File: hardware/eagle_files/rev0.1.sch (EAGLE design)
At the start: 30 parts, among them U1 AD8332ACPZ-R7, U2 AD8333ACPZ-REEL, U3 AD8021ARMZ, U4 AD8021ARMZ

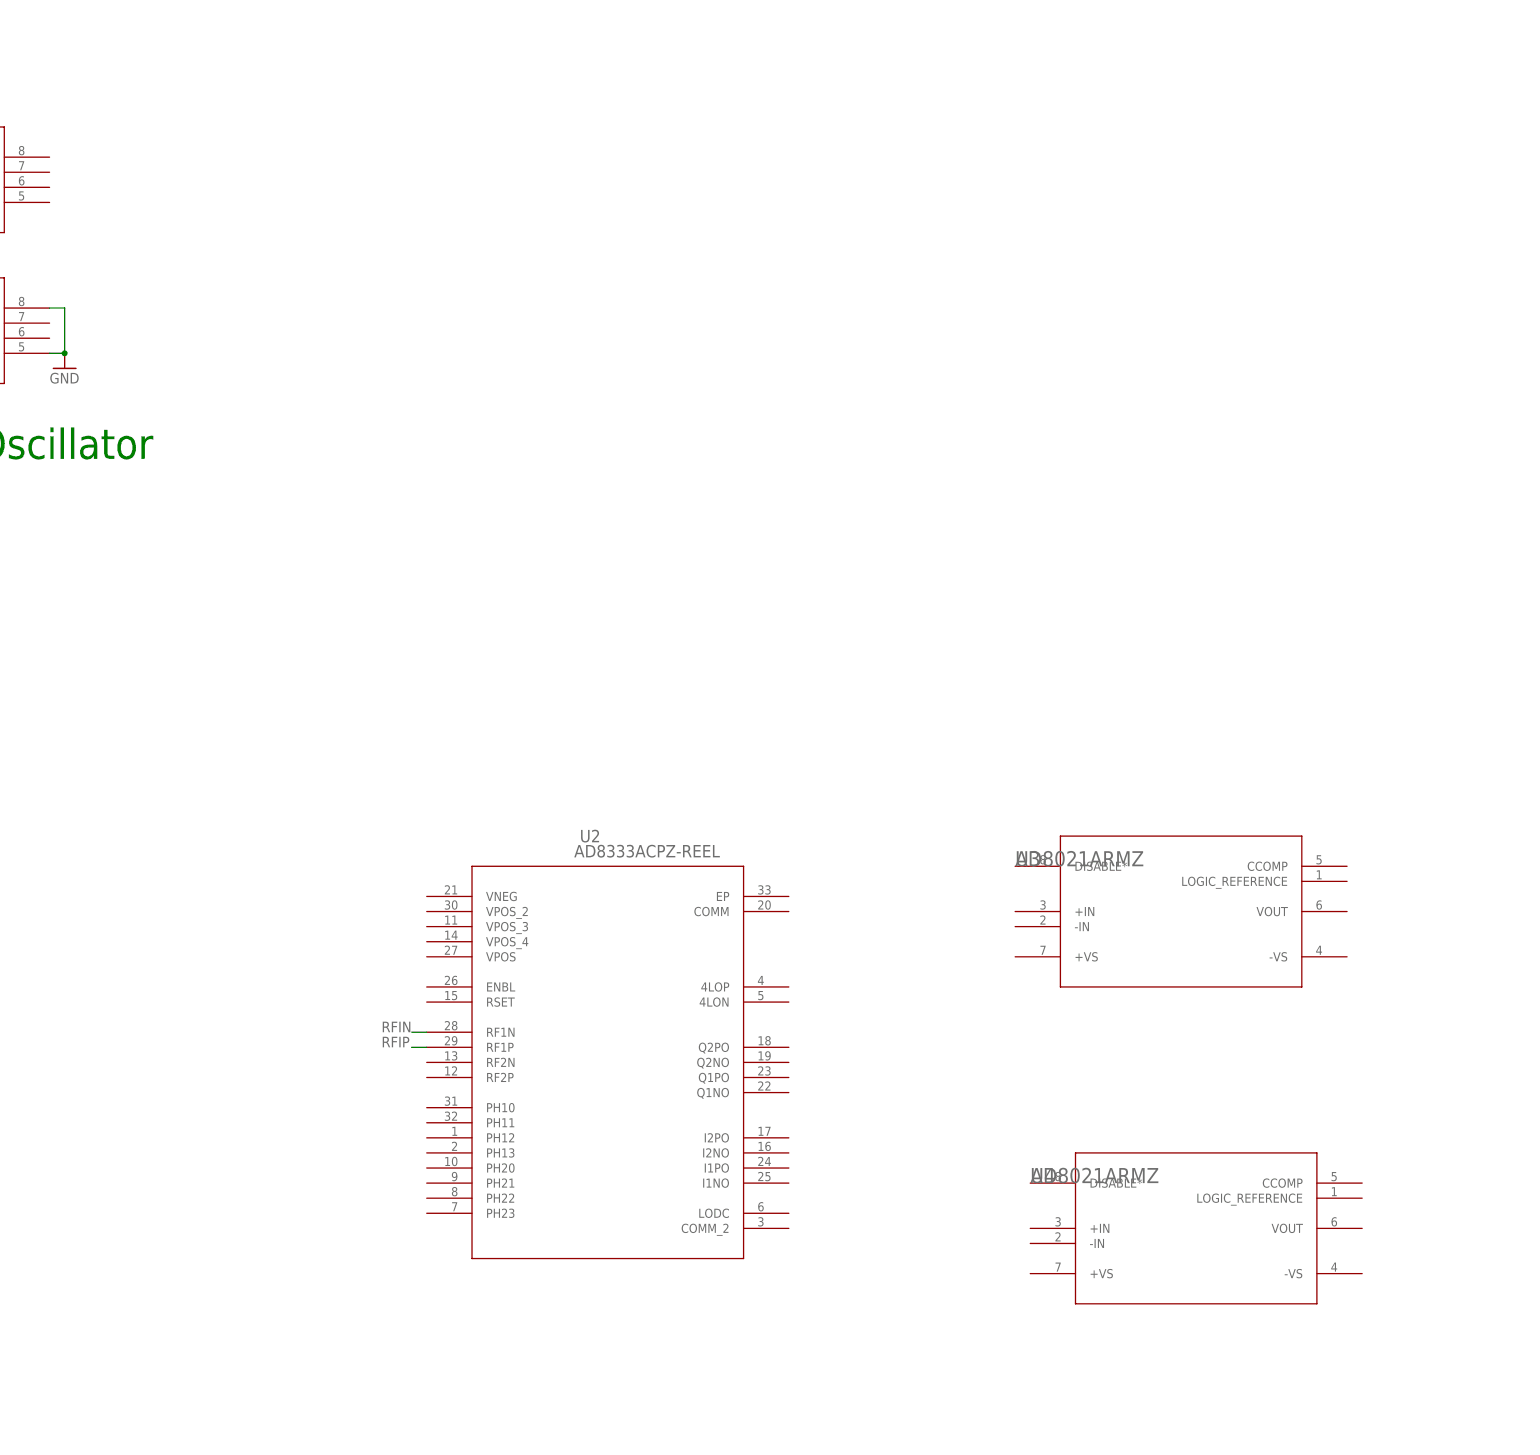
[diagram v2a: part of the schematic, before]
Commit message: Added AD8333
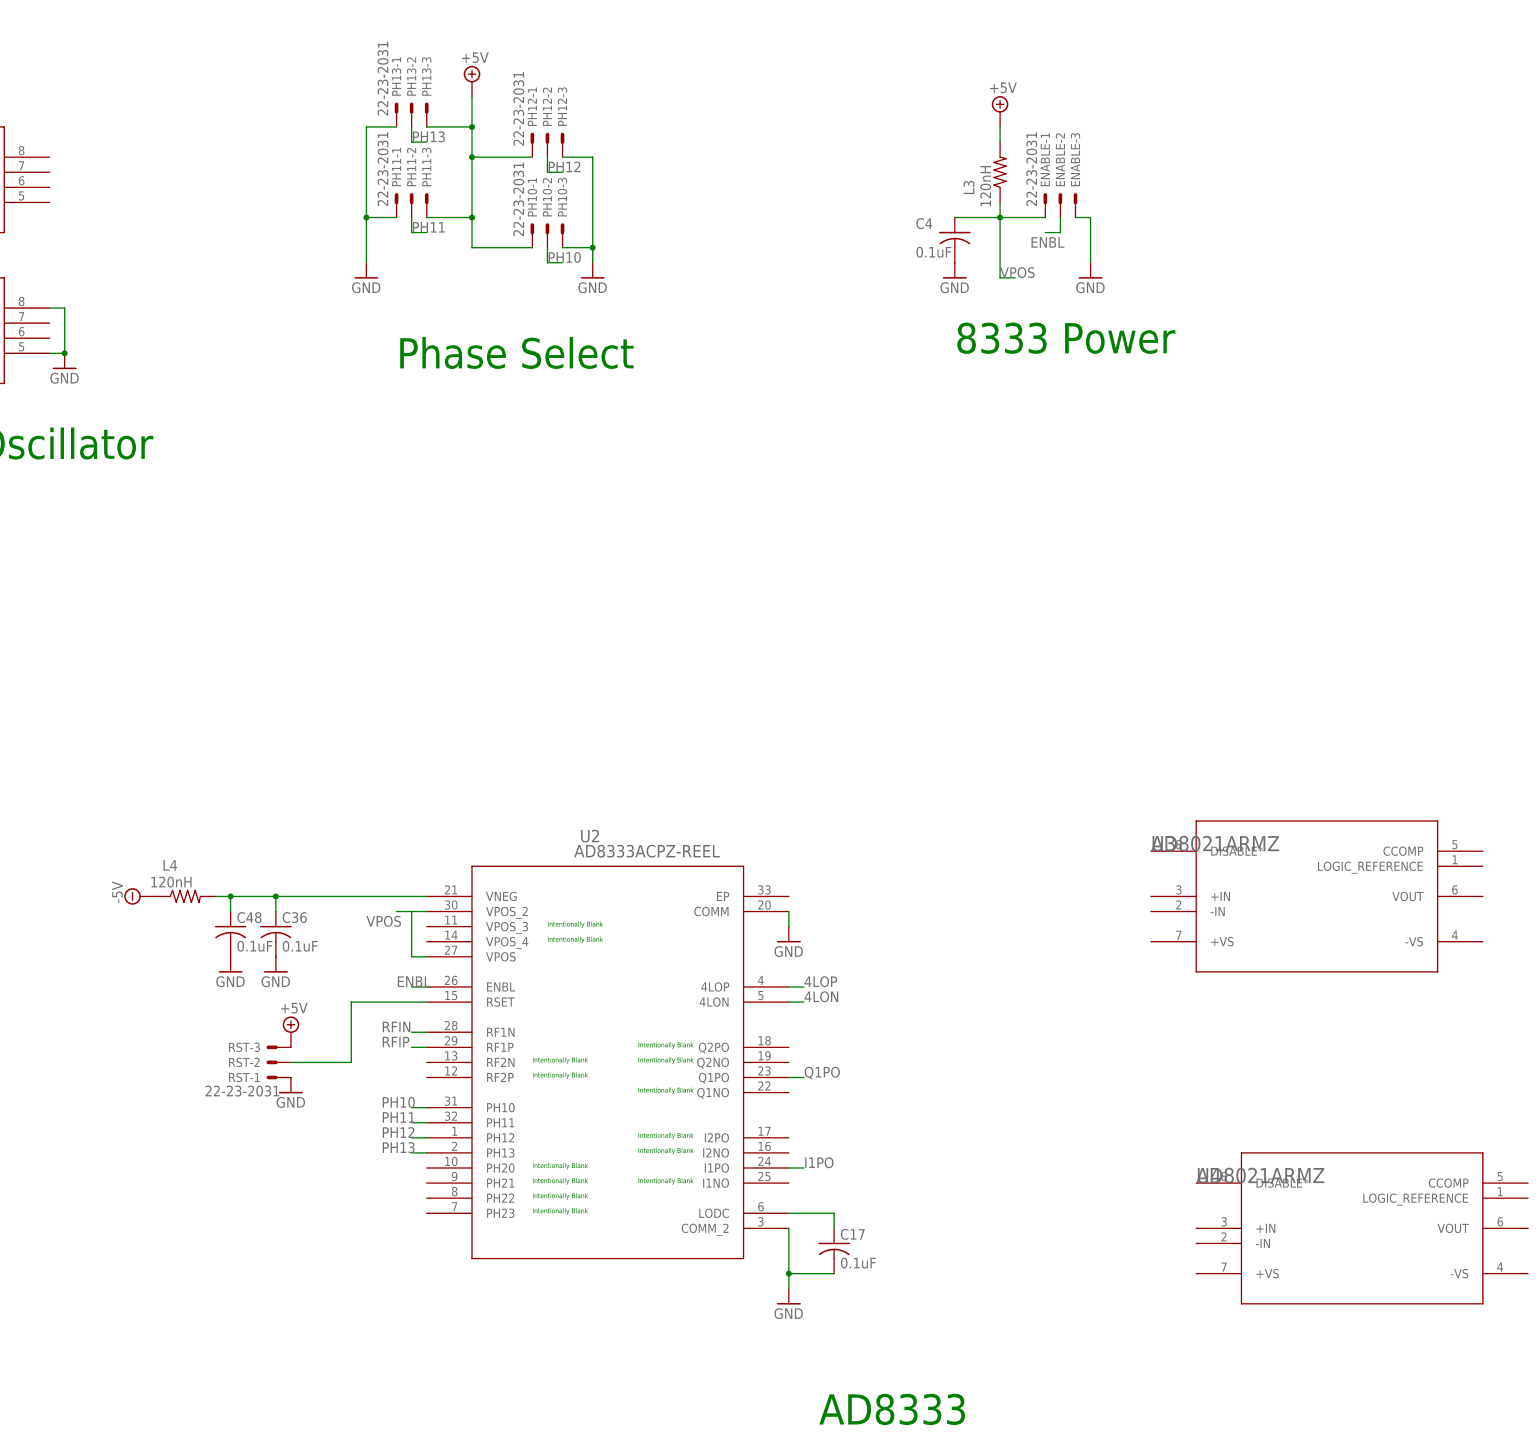
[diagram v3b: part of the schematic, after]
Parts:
- added C17, C36, C4, C48: 0.1uF, resistor:C-USC1206
- added ENABLE, PH10, PH11, PH12, PH13, RST: 22-23-2031, con-molex:22-23-2031
- added L3, L4: 120nH, resistor:R-US_R0603
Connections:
- new net -5V: L4.1
- new net ENBL: ENABLE-2.S, U2.ENBL
- new net I1PO: U2.I1PO
- new net N$10: C17.1, U2.LODC
- new net N$11: RST-2.S, U2.RSET
- new net N$9: C36.1, C48.1, L4.2, U2.VNEG
- new net PH10: PH10-2.S, U2.PH10
- new net PH11: PH11-2.S, U2.PH11
- new net PH12: PH12-2.S, U2.PH12
- new net PH13: PH13-2.S, U2.PH13
- new net Q1PO: U2.Q1PO
- new net VPOS: C4.1, ENABLE-1.S, L3.1, U2.VPOS, U2.VPOS_2
- net +5V: now also L3.2, PH10-1.S, PH11-3.S, PH12-1.S, PH13-3.S, RST-3.S
- net 4LON: now also U2.4LON
- net 4LOP: now also U2.4LOP
- net GND: now also C17.2, C36.2, C4.2, C48.2, ENABLE-3.S, PH10-3.S, PH11-1.S, PH12-3.S, PH13-1.S, RST-1.S, U2.COMM, U2.COMM_2
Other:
- note added: "8333 Power"
- note added: "AD8333"
- note added: "Phase Select"
- moved on the sheet: U3, U4

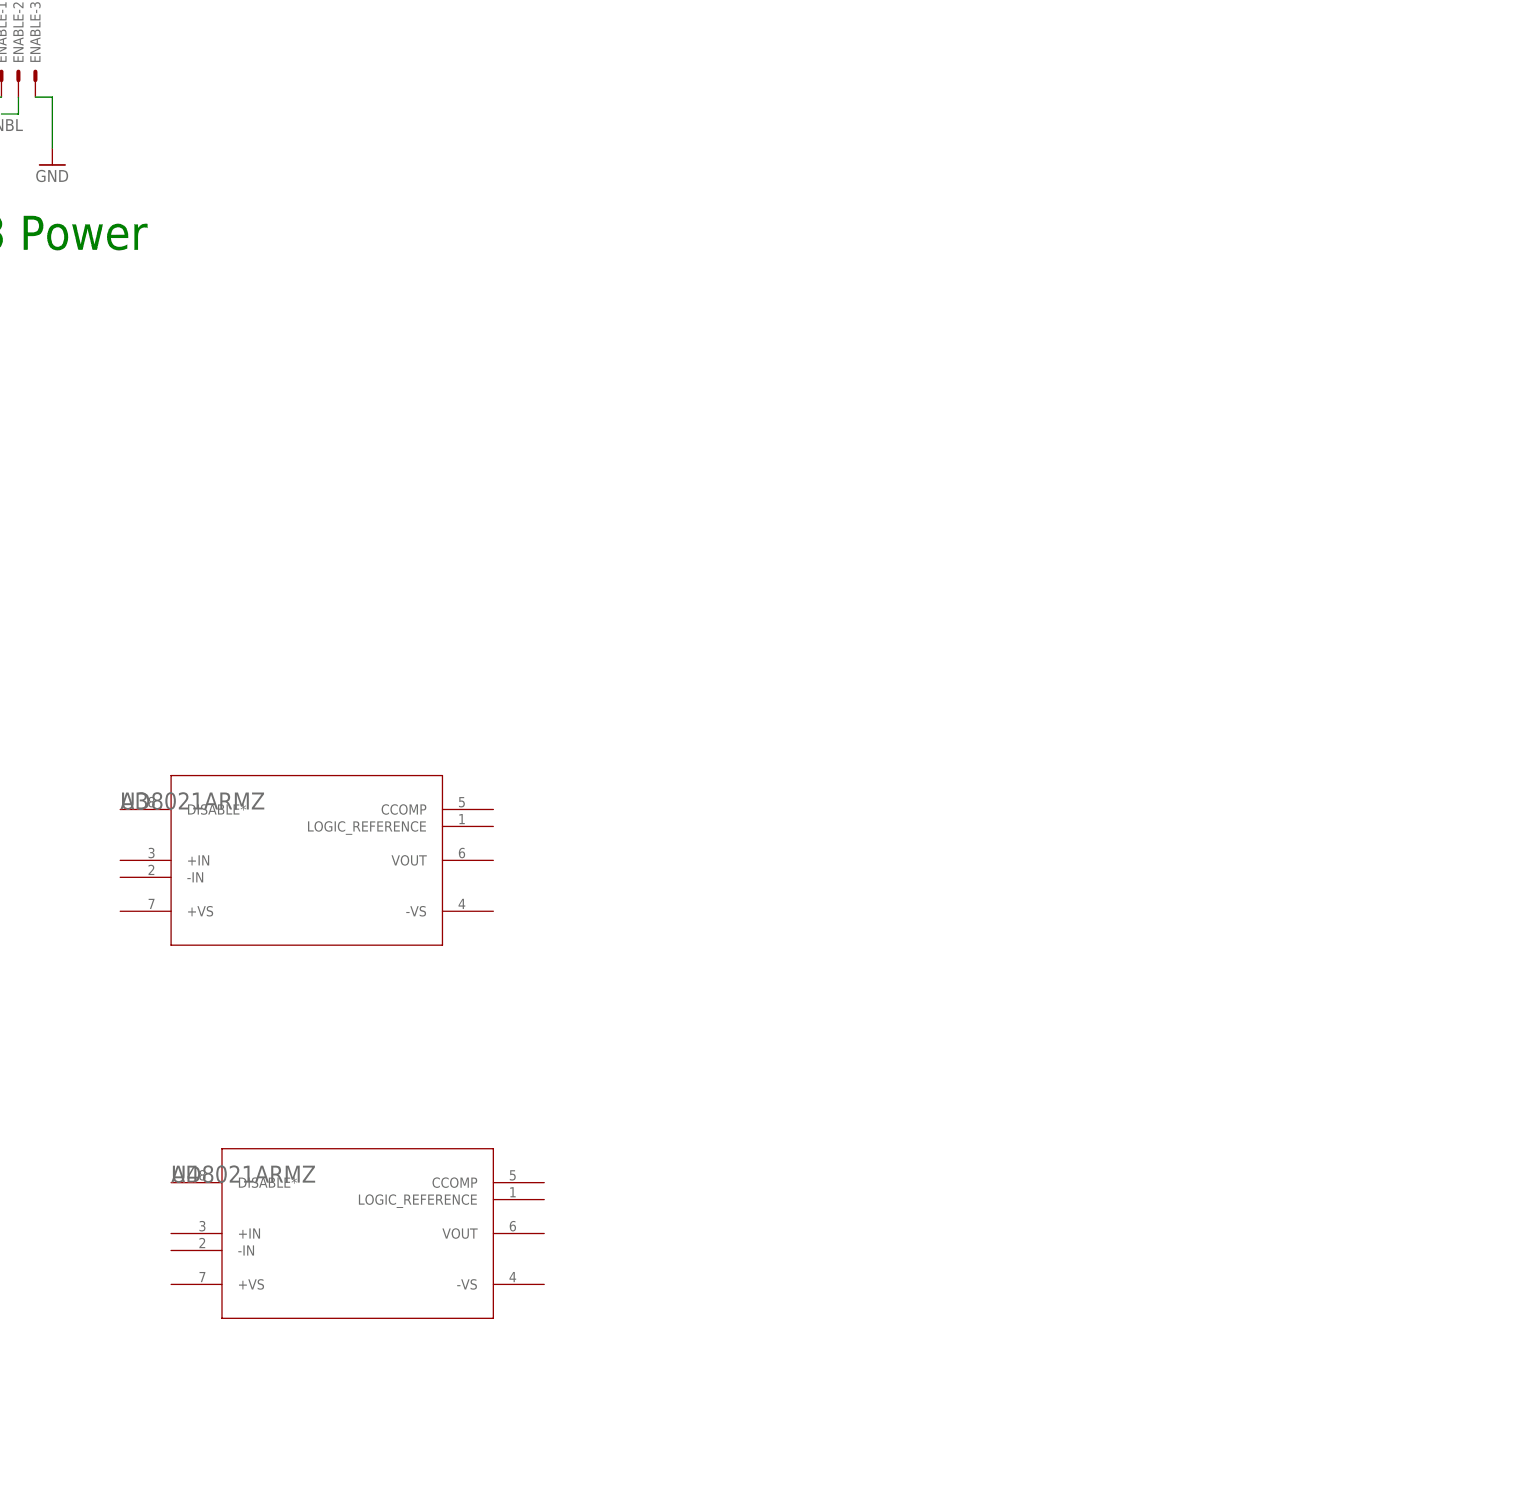
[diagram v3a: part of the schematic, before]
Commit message: Added AD8021 x 2
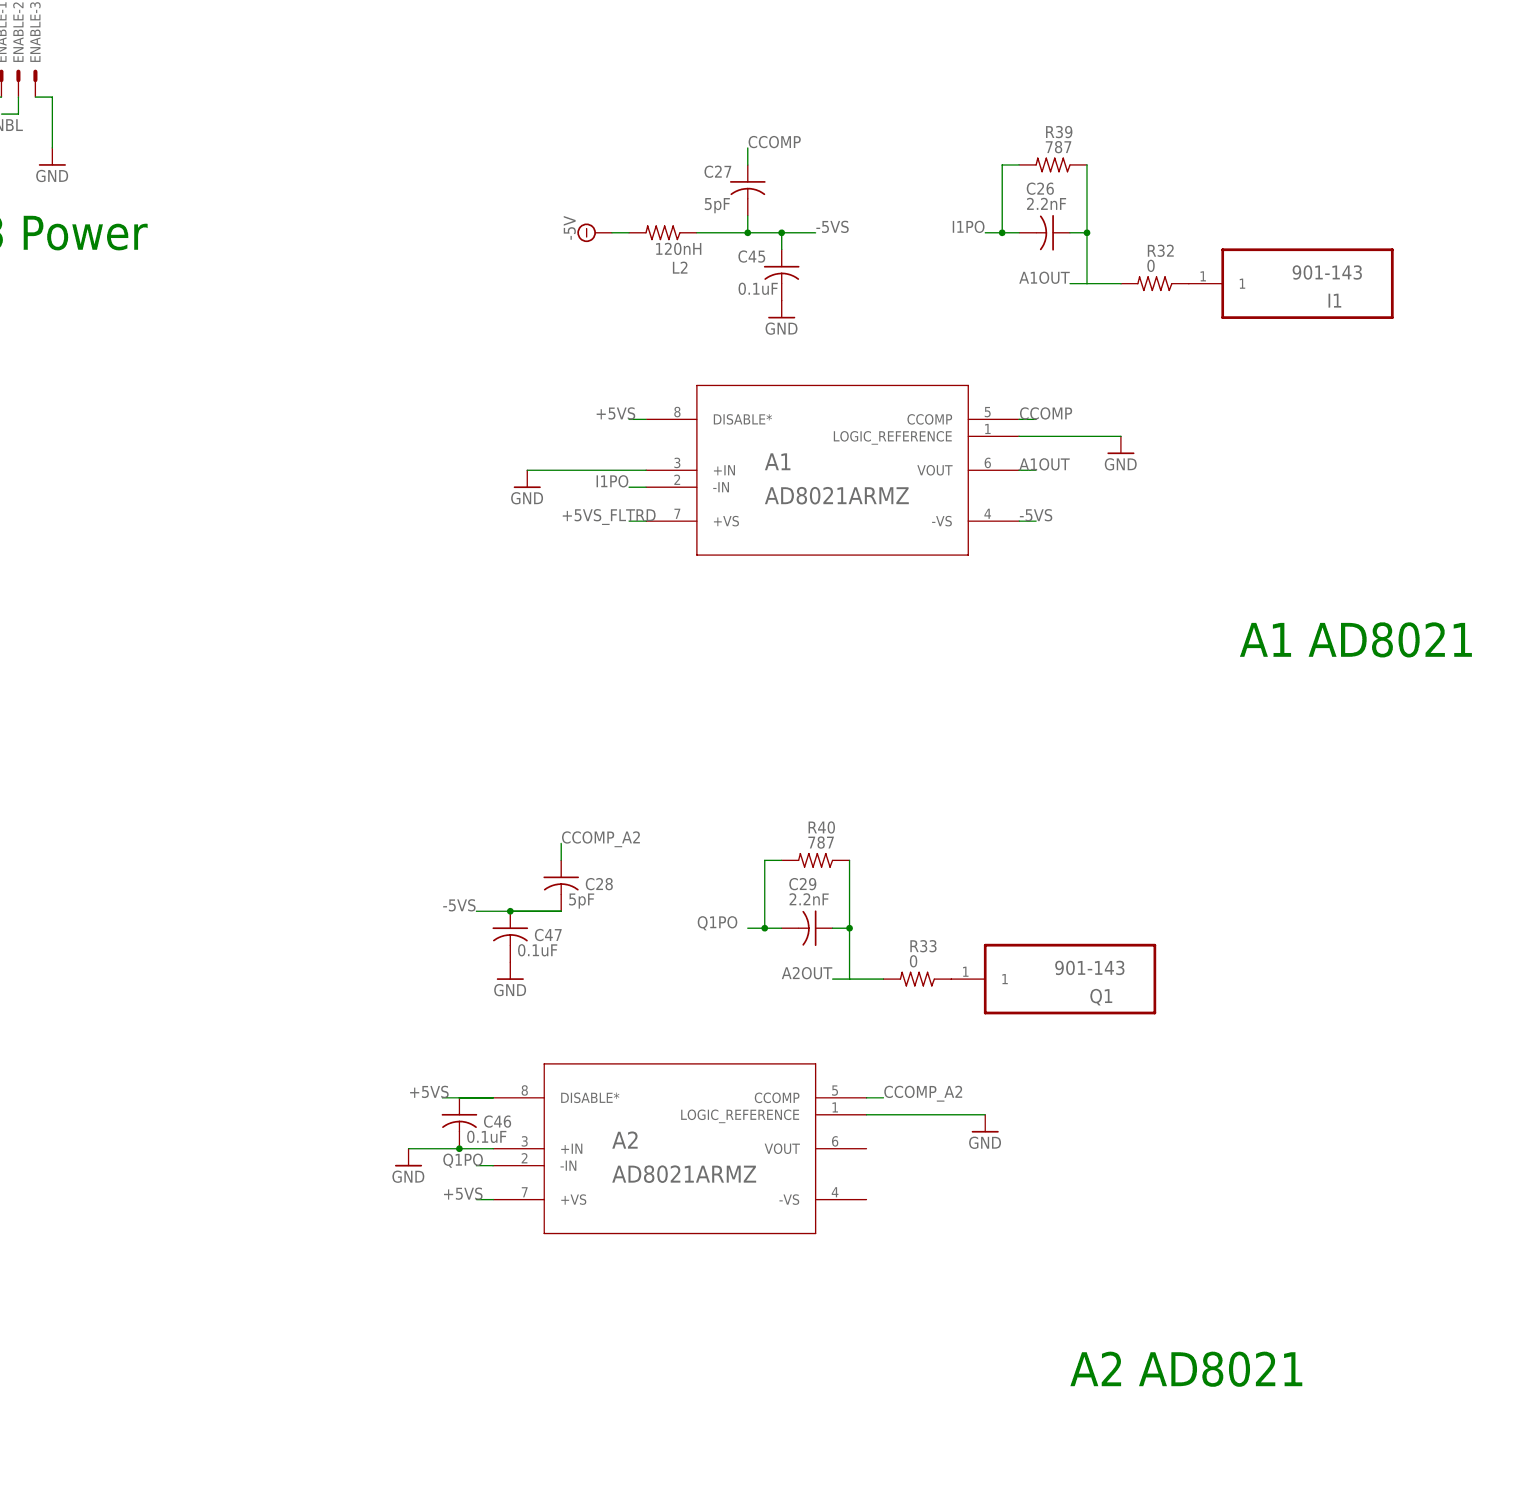
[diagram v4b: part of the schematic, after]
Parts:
- removed U3, U4: AD8021ARMZ, ad8021:AD8021ARMZ
- added A1, A2: AD8021ARMZ, ad8021:AD8021ARMZ
- added C26, C29: 2.2nF, resistor:C-USC1206
- added C27, C28: 5pF, resistor:C-USC1206
- added C45, C46, C47: 0.1uF, resistor:C-USC1206
- added I1, Q1: 901-143, Amphenol_By_element14_Batch_1:901-143
- added L2: 120nH, resistor:R-US_R0603
- added R32, R33: 0, resistor:R-US_R1206
- added R39, R40: 787, resistor:R-US_R1206
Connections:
- new net +5VS: A1.DISABLE*, A2.+VS, A2.DISABLE*, C46.1
- new net +5VS_FLTRD: A1.+VS
- new net -5VS: A1.-VS, C27.2, C28.2, C45.1, C47.1, L2.1
- new net A1OUT: A1.VOUT, C26.1, R32.2, R39.1
- new net A2OUT: C29.1, R33.2, R40.1
- new net CCOMP: A1.CCOMP, C27.1
- new net CCOMP_A2: A2.CCOMP, C28.1
- new net N$12: Q1.1, R33.1
- new net N$13: I1.1, R32.1
- net -5V: now also L2.2
- net GND: now also A1.+IN, A1.LOGIC_REFERENCE, A2.+IN, A2.LOGIC_REFERENCE, C45.2, C46.2, C47.2
- net I1PO: now also A1.-IN, C26.2, R39.2
- net Q1PO: now also A2.-IN, C29.2, R40.2
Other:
- note added: "A1 AD8021"
- note added: "A2 AD8021"

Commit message: revision 0.1 complete: Included in this upload is an html version of the BOM
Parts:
- removed I1, Q1: 901-143, Amphenol_By_element14_Batch_1:901-143
- removed L2: 120nH, resistor:R-US_R0603
- added +5V_IN, -5V_IN, JP1, JP2, JP3, JP4: M023.5MM, SparkFun-Connectors:M023.5MM
- added C44: 0.1uF, resistor:C-USC1206
- added JP5, JP6: (no value), SparkFun-Connectors:AUDIO-JACKPTH
- added L6, L7: 120nH, resistor:R-US_R0603
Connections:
- removed net N$12: Q1.1, R33.1
- removed net N$13: I1.1, R32.1
- new net I_CH_OUT: JP5.LEFT, JP6.RIGHT, R32.1
- new net Q_CH_OUT: JP5.RIGHT, JP6.LEFT, R33.1
- net +5V: now also +5V_IN.1, +5V_IN.2, L6.1
- net +5VS: now also C44.1, L6.2
- net -5V: now also -5V_IN.1, -5V_IN.2, L7.2; no longer L2.2
- net -5VS: now also A2.-VS, L7.1; no longer L2.1
- net A2OUT: now also A2.VOUT
- net GND: now also C44.2, JP1.1, JP1.2, JP2.1, JP2.2, JP3.1, JP3.2, JP4.1, JP4.2, JP5.SLEEVE, JP6.SLEEVE, U2.EP
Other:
- note added: "I/O"
- moved on the sheet: A1, A2, C1, C11, C13, C14, C17, C2, C26, C27, C28, C29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
